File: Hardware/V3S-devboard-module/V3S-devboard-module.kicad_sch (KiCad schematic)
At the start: 4 parts, among them CN1 AS0A826-H2RB-7H, J1 Bus_DDR4_Edge_Conn

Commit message: Started working in schematic
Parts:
- removed A1: Bus_DDR4_Edge_Conn, lpddr4-testbed-footprints:Bus_DDR4_Conn_Edge, symbol lpddr4-testbed:Bus_DDR4_Edge_Conn
- removed J1: Bus_DDR4_Edge_Conn, SODIMM-DDR4:Bus_DDR4_Conn_Edge, symbol lpddr4-testbed:Bus_DDR4_Edge_Conn
- removed R1: R_US, Resistor_SMD:R_0402_1005Metric_Pad0.72x0.64mm_HandSolder, symbol Device:R_US
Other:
- added sheet DIMM (DIMM.kicad_sch)
- added sheet power (power.kicad_sch)
- added sheet uP (uP.kicad_sch)
- moved on the sheet: CN1

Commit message: more schematic changes
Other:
- sheet uP ports: added ETH0{ETH}; removed none
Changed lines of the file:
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@@
 	(generator_version "8.0")
 	(paper "A3")
+	(bus
+		(pts
+			(xy 207.01 110.49) (xy 213.36 110.49)
+		)
+		(stroke
+			(width 0)
+			(type default)
+		)
+	)
 	(symbol
 		(lib_id "SODIMM-socket-AS0A826-H2RB-7H:AS0A826-H2RB-7H")
@@
 	)
 	(sheet
-		(at 224.79 96.52)
-		(size 53.34 29.21)
+		(at 213.36 104.14)
+		(size 49.53 34.29)
 		(fields_autoplaced yes)
 		(stroke
@@
 		)
 		(property "Sheetname" "uP"
-			(at 224.79 95.8084 0)
+			(at 213.36 103.4284 0)
 			(effects
 				(font
@@
 		)
 		(property "Sheetfile" "uP.kicad_sch"
-			(at 224.79 126.3146 0)
+			(at 213.36 139.0146 0)
 			(effects
 				(font
@@
 			)
 		)
+		(pin "ETH0{ETH}" input
+			(at 213.36 110.49 180)
+			(effects
+				(font
+					(size 1.27 1.27)
+				)
+				(justify left)
+			)
+		)

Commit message: schematic improvements
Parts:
- CN1: footprint SODIMM:SODIMM_DDR4_EDGE -> SODIMM-socket-AS0A826-H2RB-7H:CONN-SMD_AS0A826-H2RB-7H
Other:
- sheet uP ports: added none; removed ETH0{ETH}
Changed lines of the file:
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@@
 	(generator_version "8.0")
 	(paper "A3")
-	(bus
-		(pts
-			(xy 207.01 110.49) (xy 213.36 110.49)
-		)
-		(stroke
-			(width 0)
-			(type default)
-		)
-	)
 	(symbol
 		(lib_id "SODIMM-socket-AS0A826-H2RB-7H:AS0A826-H2RB-7H")
@@
 			)
 		)
-		(property "Footprint" "SODIMM:SODIMM_DDR4_EDGE"
+		(property "Footprint" "SODIMM-socket-AS0A826-H2RB-7H:CONN-SMD_AS0A826-H2RB-7H"
 			(at 236.22 354.33 0)
 			(effects
@@
 	)
 	(sheet
-		(at 97.79 161.29)
+		(at 219.71 92.71)
 		(size 50.8 36.83)
 		(fields_autoplaced yes)
@@
 		)
 		(property "Sheetname" "power"
-			(at 97.79 160.5784 0)
+			(at 219.71 91.9984 0)
 			(effects
 				(font
@@
 		)
 		(property "Sheetfile" "power.kicad_sch"
-			(at 97.79 198.7046 0)
+			(at 219.71 130.1246 0)
 			(effects
 				(font
@@
 	)
 	(sheet
-		(at 213.36 104.14)
+		(at 160.02 93.98)
 		(size 49.53 34.29)
 		(fields_autoplaced yes)
@@
 		)
 		(property "Sheetname" "uP"
-			(at 213.36 103.4284 0)
+			(at 160.02 93.2684 0)
 			(effects
 				(font
@@
 		)
 		(property "Sheetfile" "uP.kicad_sch"
-			(at 213.36 139.0146 0)
+			(at 160.02 128.8546 0)
 			(effects
 				(font
@@
 			)
 		)
-		(pin "ETH0{ETH}" input
-			(at 213.36 110.49 180)
-			(effects
-				(font
-					(size 1.27 1.27)
-				)
-				(justify left)
-			)
-		)

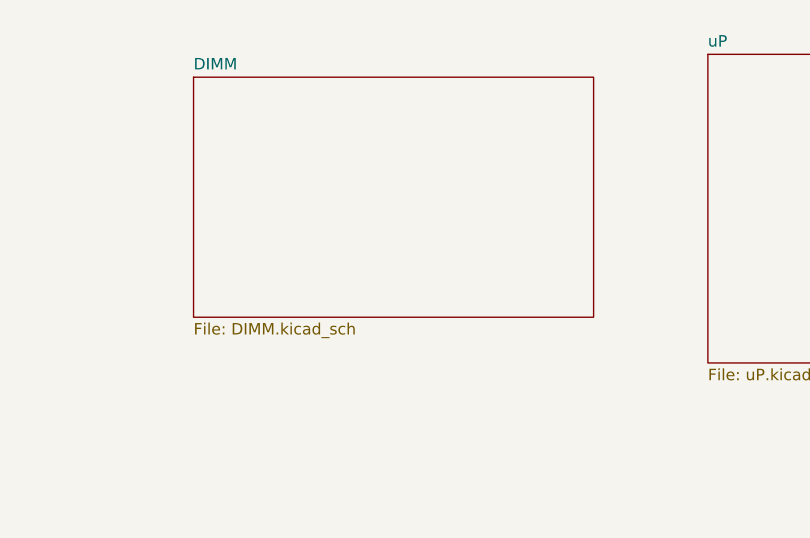
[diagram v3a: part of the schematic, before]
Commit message: Removed old project. Schematic improvements
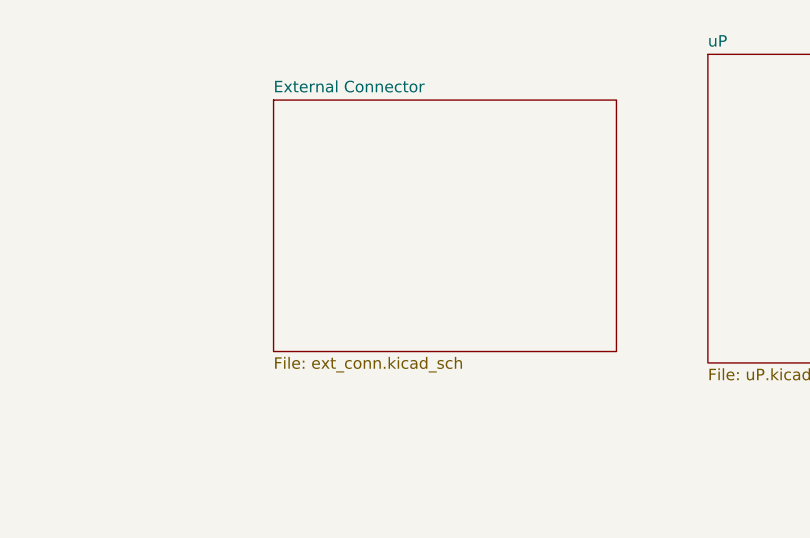
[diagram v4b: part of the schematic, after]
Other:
- removed sheet DIMM
- added sheet External Connector (ext_conn.kicad_sch)
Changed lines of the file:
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@@
+	)
+	(sheet
+		(at 111.76 99.06)
+		(size 38.1 27.94)
+		(fields_autoplaced yes)
+		(stroke
+			(width 0.1524)
+			(type solid)
+		)
+		(fill
+			(color 0 0 0 0.0000)
+		)
+		(property "Sheetname" "External Connector"
+			(at 111.76 98.3484 0)
+			(effects
+				(font
+					(size 1.27 1.27)
+				)
+				(justify left bottom)
+			)
+		)
+		(property "Sheetfile" "ext_conn.kicad_sch"
+			(at 111.76 127.5846 0)
+			(effects
+				(font
+					(size 1.27 1.27)
+				)
+				(justify left top)
+			)
+		)
+		(instances
+			(project "V3S-devboard-module"
+				(path "/5d41c08e-2331-42df-a2d5-1aeb6ed4388c"
+					(page "4")
+				)
+			)
+		)
 	)
 	(sheet
@@
 		(property "Sheetfile" "power.kicad_sch"
 			(at 219.71 130.1246 0)
-			(effects
-				(font
-					(size 1.27 1.27)
-				)
-				(justify left top)
-			)
-		)
-		(instances
-			(project "V3S-devboard-module"
-				(path "/5d41c08e-2331-42df-a2d5-1aeb6ed4388c"
-					(page "3")
-				)
-			)
-		)
-	)
-	(sheet
-		(at 102.87 96.52)
-		(size 44.45 26.67)
-		(fields_autoplaced yes)
-		(stroke
-			(width 0.1524)
-			(type solid)
-		)
-		(fill
-			(color 0 0 0 0.0000)
-		)
-		(property "Sheetname" "DIMM"
-			(at 102.87 95.8084 0)
-			(effects
-				(font
-					(size 1.27 1.27)
-				)
-				(justify left bottom)
-			)
-		)
-		(property "Sheetfile" "DIMM.kicad_sch"
-			(at 102.87 123.7746 0)
 			(effects
 				(font
@@
 			(project "V3S-devboard-module"
 				(path "/5d41c08e-2331-42df-a2d5-1aeb6ed4388c"
-					(page "4")
+					(page "2")
 				)
 			)

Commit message: general improvements. power almost complete
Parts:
- removed CN1: AS0A826-H2RB-7H, SODIMM-socket-AS0A826-H2RB-7H:CONN-SMD_AS0A826-H2RB-7H, symbol SODIMM-socket-AS0A826-H2RB-7H:AS0A826-H2RB-7H
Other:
- sheet power renamed Power

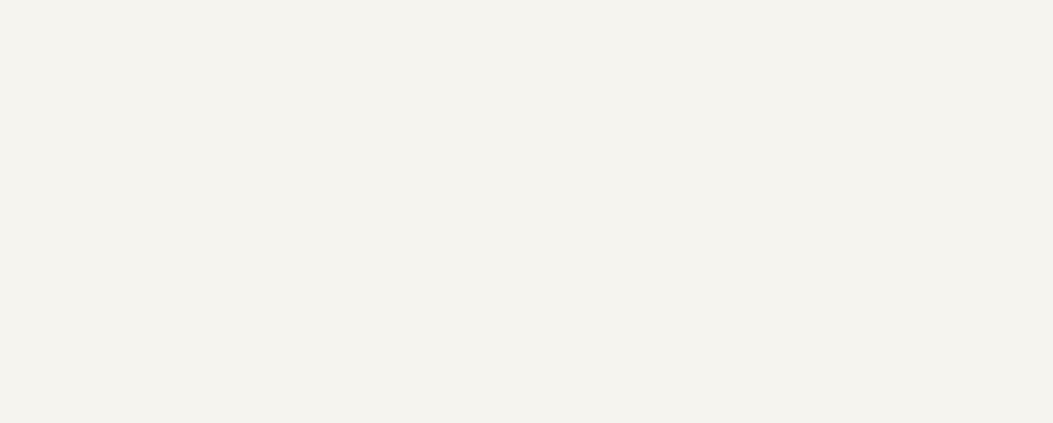
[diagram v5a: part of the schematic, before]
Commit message: CPU schematic improvements
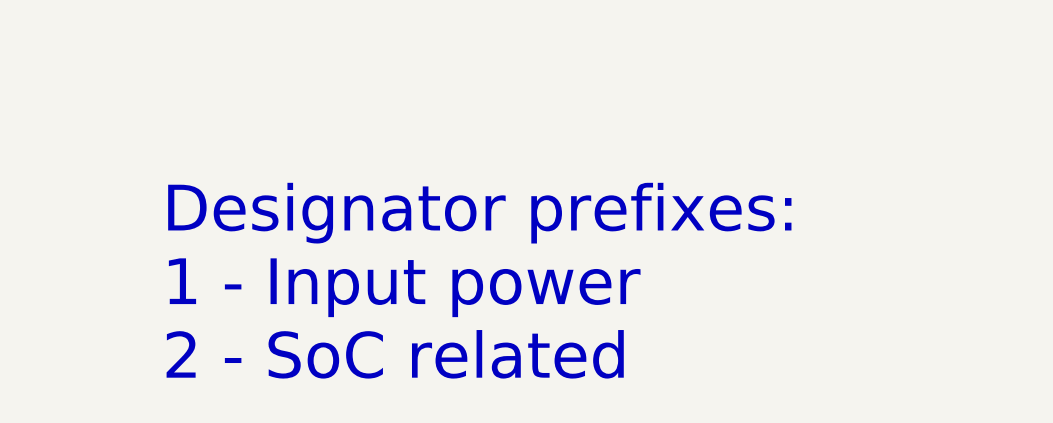
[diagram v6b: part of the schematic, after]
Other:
- note added: "Designator prefixes: 1 - Input power 2 - SoC related"
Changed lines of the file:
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@@
 		(date "2024-03-23")
+	)
+	(text "Designator prefixes:\n1 - Input power\n2 - SoC related\n"
+		(exclude_from_sim no)
+		(at 305.054 203.708 0)
+		(effects
+			(font
+				(size 5.08 5.08)
+			)
+			(justify left)
+		)
 	)
 	(sheet
@@
 			(project "V3S-devboard-module"
 				(path "/5d41c08e-2331-42df-a2d5-1aeb6ed4388c"
-					(page "3")
+					(page "2")
 				)
 			)
@@
 			(project "V3S-devboard-module"
 				(path "/5d41c08e-2331-42df-a2d5-1aeb6ed4388c"
-					(page "2")
+					(page "3")
 				)
 			)
